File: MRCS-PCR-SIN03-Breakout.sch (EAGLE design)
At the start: 6 parts

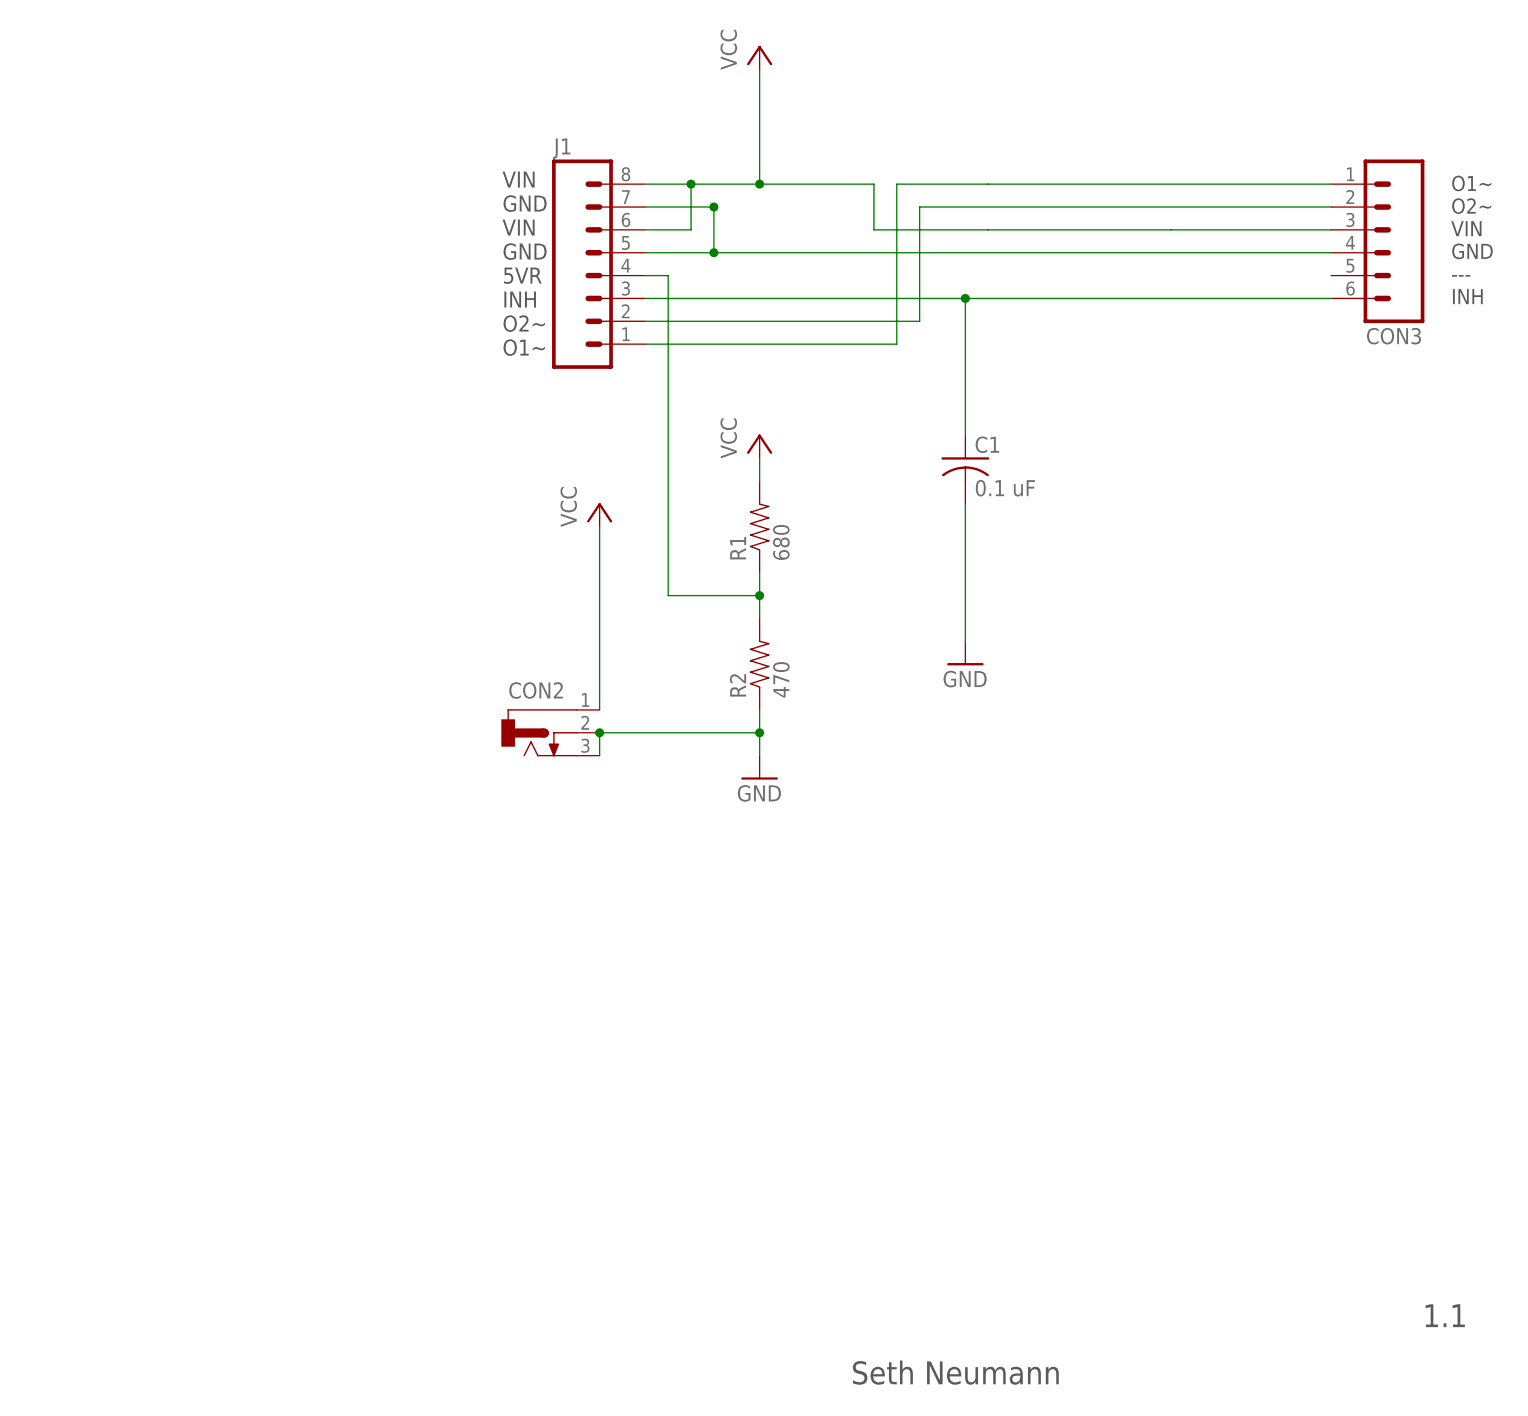
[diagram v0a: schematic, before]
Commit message: Added 8 mm screw barrier block
this might be more useful for the phone folks as it supports spade lugs. Plenty of room on the board!
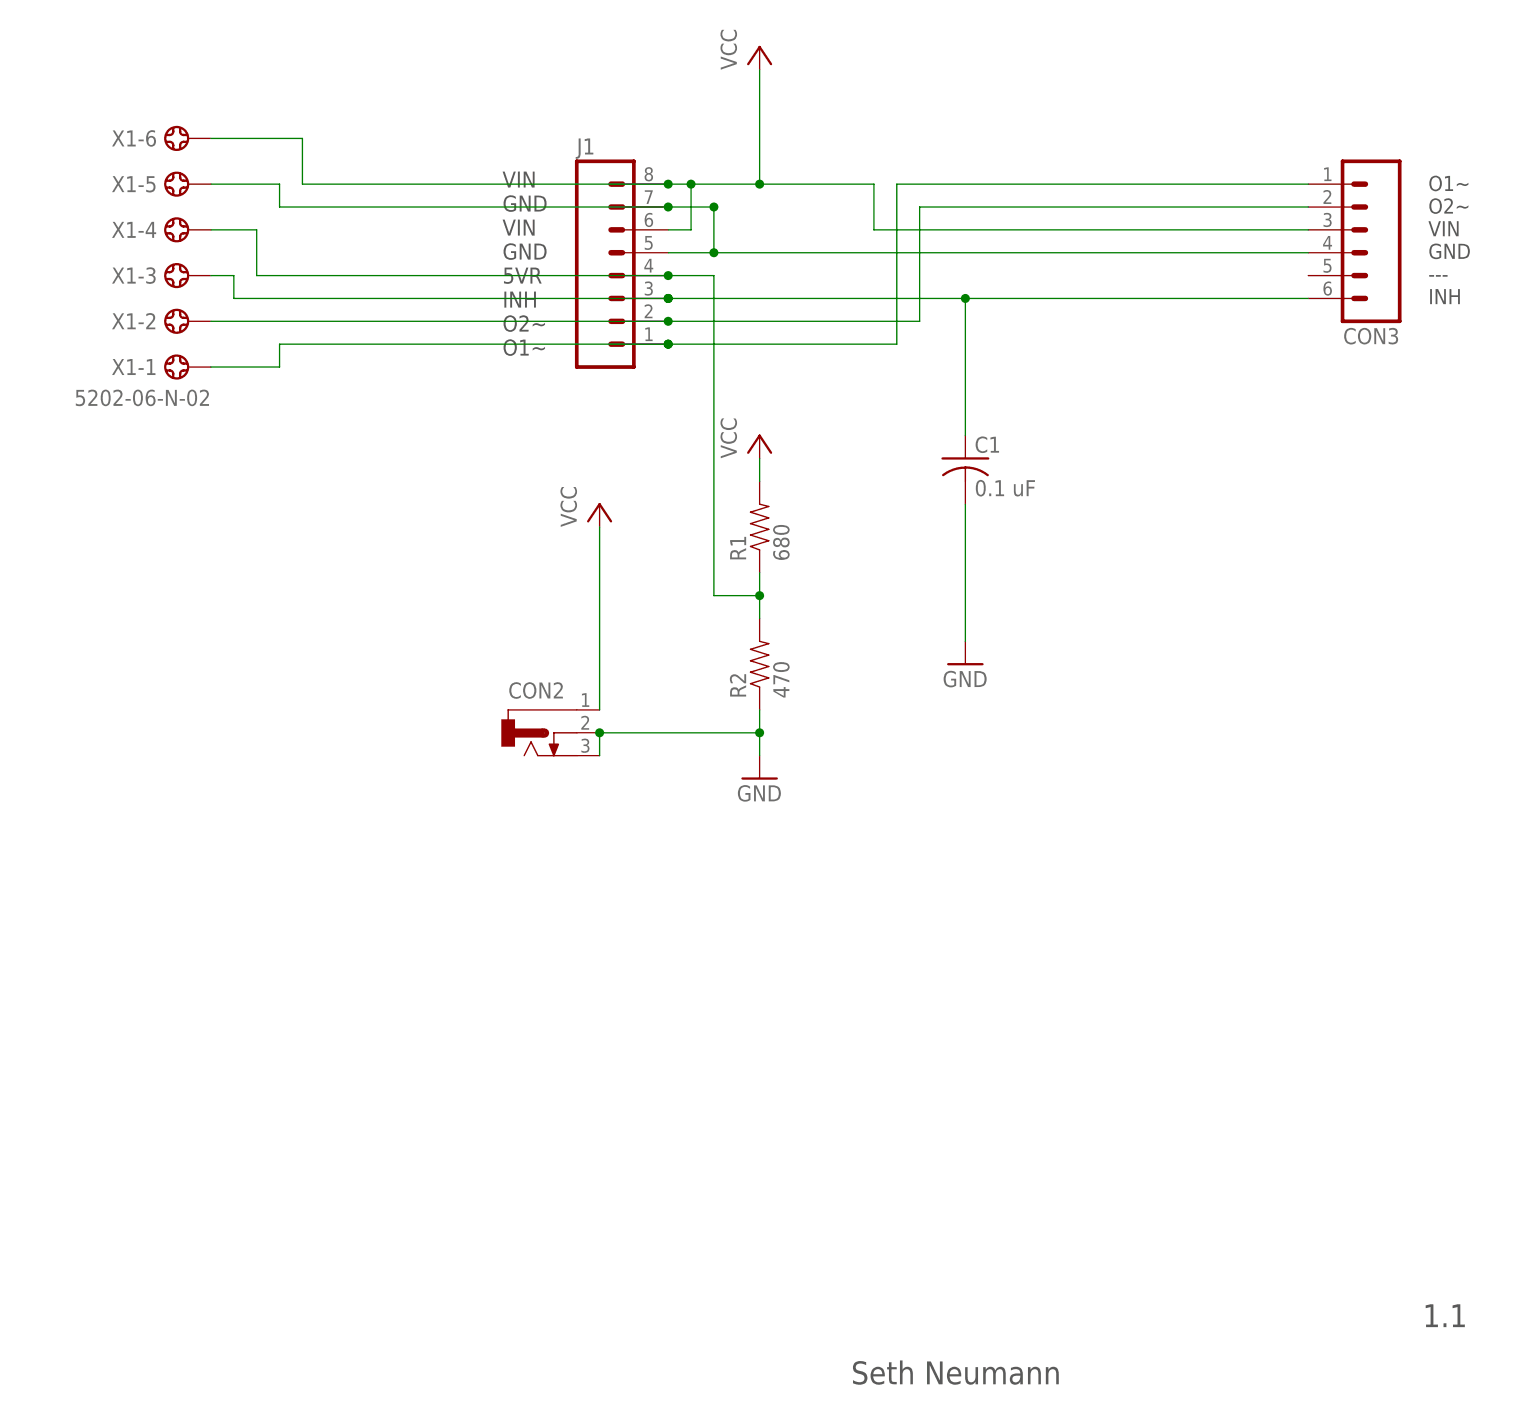
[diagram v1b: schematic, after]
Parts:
- added X1: 5202-06-N-02, con-ebyelectro:5202-06-N-02
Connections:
- net 5VR: now also X1-4.1
- net GND: now also CON3.4, X1-5.1
- net INH: now also X1-3.1
- net O1: now also X1-1.1
- net O2: now also X1-2.1
- net VCC: now also X1-6.1
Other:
- moved on the sheet: CON3, J1
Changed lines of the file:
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@@
 <part name="CON3" library="SPCoast" deviceset="CONNECTOR-M06" device="POLAR"/>
 <part name="P+3" library="SPCoast" deviceset="VCC" device=""/>
+<part name="X1" library="con-ebyelectro" deviceset="5202-06-N-02" device=""/>
 </parts>
 <sheets>
@@
 O2~
 O1~</text>
-<text x="241.935" y="126.365" size="1.6764" layer="97">O1~
+<text x="239.395" y="126.365" size="1.6764" layer="97">O1~
 O2~
 VIN
@@
 </plain>
 <instances>
-<instance part="J1" gate="G$1" x="147.32" y="129.54"/>
+<instance part="J1" gate="G$1" x="149.86" y="129.54"/>
 <instance part="R1" gate="R" x="165.1" y="101.6" rot="R90"/>
 <instance part="R2" gate="R" x="165.1" y="86.36" rot="R90"/>
@@
 <instance part="P+1" gate="VCC" x="165.1" y="154.94"/>
 <instance part="P+2" gate="VCC" x="147.32" y="104.14"/>
-<instance part="CON3" gate="J" x="233.68" y="134.62" rot="R180"/>
+<instance part="CON3" gate="J" x="231.14" y="134.62" rot="R180"/>
 <instance part="P+3" gate="VCC" x="165.1" y="111.76"/>
+<instance part="X1" gate="-1" x="101.6" y="119.38" rot="R180"/>
+<instance part="X1" gate="-2" x="101.6" y="124.46" rot="R180"/>
+<instance part="X1" gate="-3" x="101.6" y="129.54" rot="R180"/>
+<instance part="X1" gate="-4" x="101.6" y="134.62" rot="R180"/>
+<instance part="X1" gate="-5" x="101.6" y="139.7" rot="R180"/>
+<instance part="X1" gate="-6" x="101.6" y="144.78" rot="R180"/>
 </instances>
 <busses>
@@
 <segment>
 <pinref part="J1" gate="G$1" pin="1"/>
-<wire x1="152.4" y1="121.92" x2="180.34" y2="121.92" width="0.4064" layer="91"/>
+<wire x1="154.94" y1="121.92" x2="180.34" y2="121.92" width="0.4064" layer="91"/>
 <wire x1="180.34" y1="121.92" x2="180.34" y2="139.7" width="0.4064" layer="91"/>
-<wire x1="180.34" y1="139.7" x2="190.5" y2="139.7" width="0.4064" layer="91"/>
-<wire x1="190.5" y1="139.7" x2="228.6" y2="139.7" width="0.4064" layer="91"/>
+<wire x1="180.34" y1="139.7" x2="226.06" y2="139.7" width="0.4064" layer="91"/>
 <pinref part="CON3" gate="J" pin="1"/>
+<wire x1="104.14" y1="119.38" x2="111.76" y2="119.38" width="0.4064" layer="91"/>
+<wire x1="111.76" y1="119.38" x2="111.76" y2="121.92" width="0.4064" layer="91"/>
+<wire x1="111.76" y1="121.92" x2="154.94" y2="121.92" width="0.4064" layer="91"/>
+<junction x="154.94" y="121.92"/>
+<junction x="154.94" y="121.92"/>
+<pinref part="X1" gate="-1" pin="1"/>
 </segment>
 </net>
@@
 <segment>
 <pinref part="J1" gate="G$1" pin="2"/>
-<wire x1="152.4" y1="124.46" x2="182.88" y2="124.46" width="0.4064" layer="91"/>
+<wire x1="154.94" y1="124.46" x2="182.88" y2="124.46" width="0.4064" layer="91"/>
 <wire x1="182.88" y1="124.46" x2="182.88" y2="137.16" width="0.4064" layer="91"/>
 <pinref part="CON3" gate="J" pin="2"/>
-<wire x1="182.88" y1="137.16" x2="228.6" y2="137.16" width="0.4064" layer="91"/>
+<wire x1="182.88" y1="137.16" x2="226.06" y2="137.16" width="0.4064" layer="91"/>
+<junction x="154.94" y="124.46"/>
+<pinref part="X1" gate="-2" pin="1"/>
+<wire x1="104.14" y1="124.46" x2="154.94" y2="124.46" width="0.4064" layer="91"/>
 </segment>
 </net>
@@
 <wire x1="187.96" y1="111.76" x2="187.96" y2="127" width="0.4064" layer="91"/>
 <pinref part="J1" gate="G$1" pin="3"/>
-<wire x1="187.96" y1="127" x2="152.4" y2="127" width="0.4064" layer="91"/>
+<wire x1="187.96" y1="127" x2="154.94" y2="127" width="0.4064" layer="91"/>
 <junction x="187.96" y="127"/>
 <pinref part="CON3" gate="J" pin="6"/>
-<wire x1="187.96" y1="127" x2="228.6" y2="127" width="0.4064" layer="91"/>
+<wire x1="187.96" y1="127" x2="226.06" y2="127" width="0.4064" layer="91"/>
+<wire x1="104.14" y1="129.54" x2="106.68" y2="129.54" width="0.4064" layer="91"/>
+<wire x1="106.68" y1="129.54" x2="106.68" y2="127" width="0.4064" layer="91"/>
+<wire x1="106.68" y1="127" x2="154.94" y2="127" width="0.4064" layer="91"/>
+<junction x="154.94" y="127"/>
+<junction x="154.94" y="127"/>
+<pinref part="X1" gate="-3" pin="1"/>
 </segment>
 </net>
@@
 <segment>
 <pinref part="J1" gate="G$1" pin="7"/>
-<wire x1="152.4" y1="137.16" x2="160.02" y2="137.16" width="0.4064" layer="91"/>
+<wire x1="154.94" y1="137.16" x2="160.02" y2="137.16" width="0.4064" layer="91"/>
 <pinref part="J1" gate="G$1" pin="5"/>
-<wire x1="160.02" y1="132.08" x2="152.4" y2="132.08" width="0.4064" layer="91"/>
+<wire x1="160.02" y1="132.08" x2="154.94" y2="132.08" width="0.4064" layer="91"/>
 <wire x1="160.02" y1="137.16" x2="160.02" y2="132.08" width="0.4064" layer="91"/>
-<wire x1="160.02" y1="132.08" x2="228.6" y2="132.08" width="0.4064" layer="91"/>
+<wire x1="160.02" y1="132.08" x2="226.06" y2="132.08" width="0.4064" layer="91"/>
 <junction x="160.02" y="137.16"/>
 <junction x="160.02" y="132.08"/>
+<pinref part="X1" gate="-5" pin="1"/>
+<wire x1="104.14" y1="139.7" x2="111.76" y2="139.7" width="0.4064" layer="91"/>
+<wire x1="111.76" y1="139.7" x2="111.76" y2="137.16" width="0.4064" layer="91"/>
+<wire x1="111.76" y1="137.16" x2="154.94" y2="137.16" width="0.4064" layer="91"/>
+<junction x="154.94" y="137.16"/>
+<pinref part="CON3" gate="J" pin="4"/>
 </segment>
 </net>
 <net name="5VR" class="0">
 <segment>
-<pinref part="J1" gate="G$1" pin="4"/>
-<wire x1="152.4" y1="129.54" x2="154.94" y2="129.54" width="0.4064" layer="91"/>
-<wire x1="154.94" y1="129.54" x2="154.94" y2="93.98" width="0.4064" layer="91"/>
 <pinref part="R1" gate="R" pin="1"/>
 <pinref part="R2" gate="R" pin="2"/>
 <wire x1="165.1" y1="96.52" x2="165.1" y2="93.98" width="0.4064" layer="91"/>
 <wire x1="165.1" y1="93.98" x2="165.1" y2="91.44" width="0.4064" layer="91"/>
-<wire x1="154.94" y1="93.98" x2="165.1" y2="93.98" width="0.4064" layer="91"/>
+<wire x1="160.02" y1="93.98" x2="165.1" y2="93.98" width="0.4064" layer="91"/>
 <junction x="165.1" y="93.98"/>
+<pinref part="X1" gate="-4" pin="1"/>
+<wire x1="104.14" y1="134.62" x2="109.22" y2="134.62" width="0.4064" layer="91"/>
+<wire x1="109.22" y1="134.62" x2="109.22" y2="129.54" width="0.4064" layer="91"/>
+<wire x1="109.22" y1="129.54" x2="154.94" y2="129.54" width="0.4064" layer="91"/>
+<wire x1="154.94" y1="129.54" x2="160.02" y2="129.54" width="0.4064" layer="91"/>
+<wire x1="160.02" y1="129.54" x2="160.02" y2="93.98" width="0.4064" layer="91"/>
+<pinref part="J1" gate="G$1" pin="4"/>
+<junction x="154.94" y="129.54"/>
 </segment>
 </net>
@@
 <segment>
 <pinref part="J1" gate="G$1" pin="8"/>
-<wire x1="152.4" y1="139.7" x2="157.48" y2="139.7" width="0.4064" layer="91"/>
+<wire x1="154.94" y1="139.7" x2="157.48" y2="139.7" width="0.4064" layer="91"/>
 <wire x1="157.48" y1="139.7" x2="157.48" y2="134.62" width="0.4064" layer="91"/>
 <pinref part="J1" gate="G$1" pin="6"/>
-<wire x1="157.48" y1="134.62" x2="152.4" y2="134.62" width="0.4064" layer="91"/>
+<wire x1="157.48" y1="134.62" x2="154.94" y2="134.62" width="0.4064" layer="91"/>
 <wire x1="157.48" y1="139.7" x2="165.1" y2="139.7" width="0.4064" layer="91"/>
 <wire x1="165.1" y1="139.7" x2="177.8" y2="139.7" width="0.4064" layer="91"/>
 <wire x1="177.8" y1="139.7" x2="177.8" y2="134.62" width="0.4064" layer="91"/>
-<wire x1="177.8" y1="134.62" x2="190.5" y2="134.62" width="0.4064" layer="91"/>
 <junction x="157.48" y="139.7"/>
 <junction x="165.1" y="139.7"/>
 <pinref part="P+1" gate="VCC" pin="VCC"/>
 <wire x1="165.1" y1="152.4" x2="165.1" y2="139.7" width="0.4064" layer="91"/>
-<wire x1="190.5" y1="134.62" x2="210.82" y2="134.62" width="0.4064" layer="91"/>
+<wire x1="177.8" y1="134.62" x2="226.06" y2="134.62" width="0.4064" layer="91"/>
 <pinref part="CON3" gate="J" pin="3"/>
-<wire x1="228.6" y1="134.62" x2="210.82" y2="134.62" width="0.4064" layer="91"/>
+<pinref part="X1" gate="-6" pin="1"/>
+<wire x1="104.14" y1="144.78" x2="114.3" y2="144.78" width="0.4064" layer="91"/>
+<wire x1="114.3" y1="144.78" x2="114.3" y2="139.7" width="0.4064" layer="91"/>
+<wire x1="114.3" y1="139.7" x2="154.94" y2="139.7" width="0.4064" layer="91"/>
+<junction x="154.94" y="139.7"/>
 </segment>
 <segment>
